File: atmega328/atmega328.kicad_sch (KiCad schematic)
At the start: 11 parts, among them SW201 default_switch, SW202 default_switch, U201 HEADER_3x2, U202 ATmega328-A, Y201 Crystal_GND2

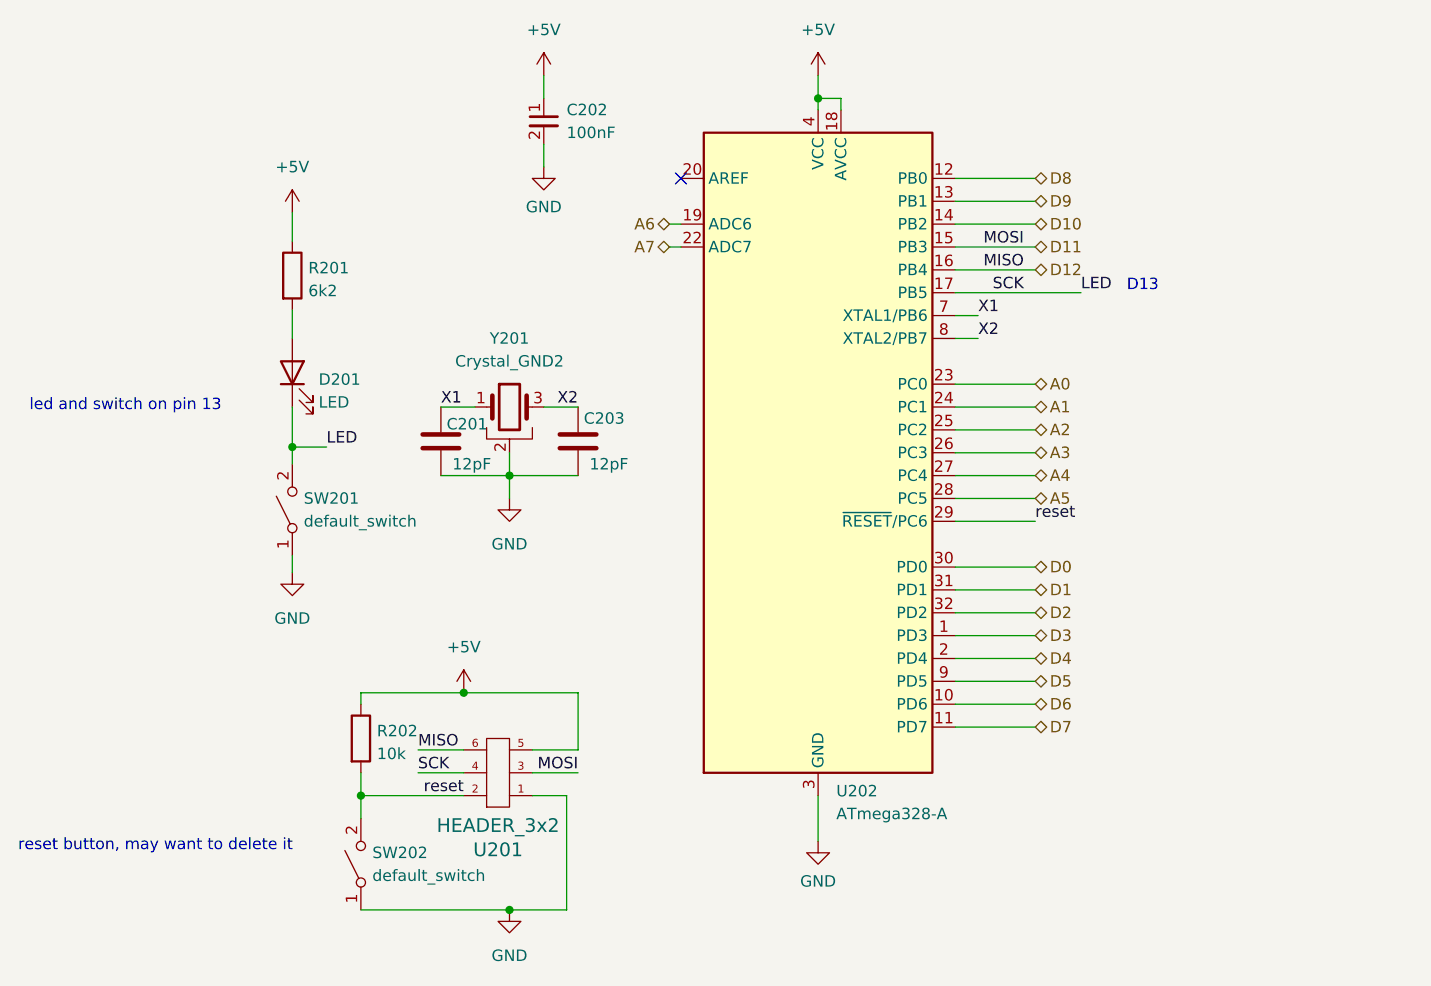
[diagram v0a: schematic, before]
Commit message: made some hierarchial label changes and updated atmega328
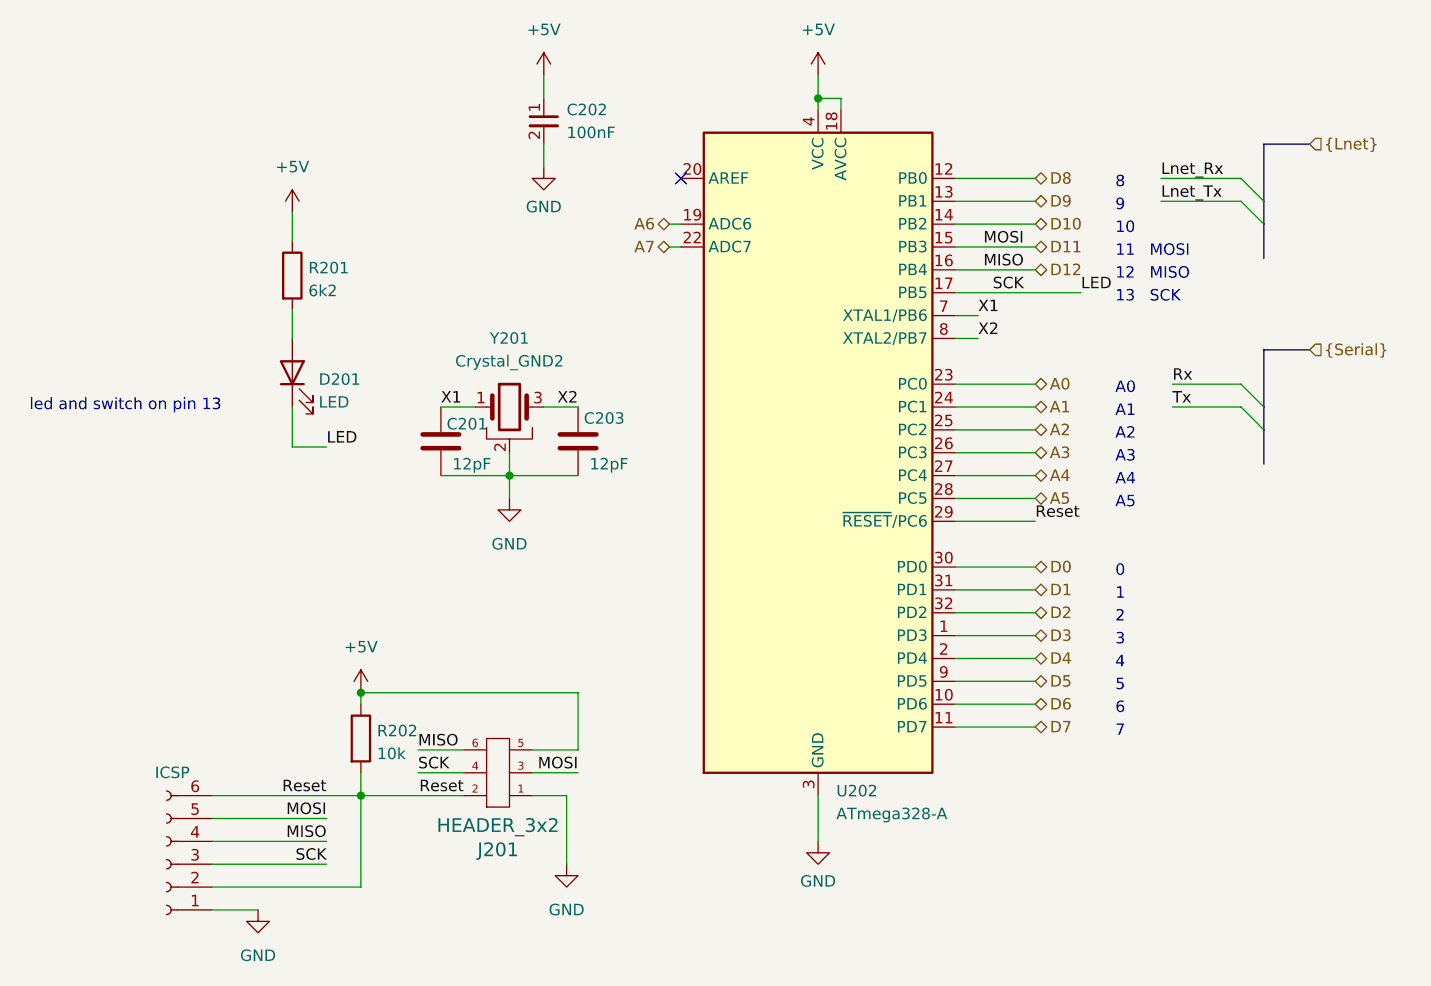
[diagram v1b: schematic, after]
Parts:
- removed SW201, SW202: default_switch, custom_kicad_lib_sk:default_switch, symbol custom_kicad_lib_sk:default_switch
- added J202: ICSP, Connector_PinHeader_2.54mm:PinHeader_1x06_P2.54mm_Vertical, symbol Connector:Conn_01x06_Socket
- renumbered U201 to J201
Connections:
- net D11: now also J202.5 (Pin_5)
- net D12: now also J202.4 (Pin_4)
- net GND: now also J202.1 (Pin_1)
- net LED: now also J202.3 (Pin_3)
- net reset renamed Reset
- net Reset: now also J202.2 (Pin_2), J202.6 (Pin_6)
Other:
- note added: "0"
- note added: "1"
- note added: "10"
- note added: "11"
- note added: "12"
- note added: "13"
- note added: "2"
- note added: "3"
- note added: "4"
- note added: "5"
- note added: "6"
- note added: "7"
- note added: "8"
- note added: "9"
- note added: "A0"
- note added: "A1"
- note added: "A2"
- note added: "A3"
- note added: "A4"
- note added: "A5"
- note added: "MISO"
- note added: "MOSI"
- note added: "SCK"
- note removed: "D13"
- note removed: "reset button, may want to delete it"
